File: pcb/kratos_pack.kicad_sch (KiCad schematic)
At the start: 94 parts, among them J1 USB_C_Receptacle_USB2.0, J2 PROG_CONN, J3 DBG_UART, J4 BAT_MID+NTC, J5 BAT_7.4V, J6 BAT_0V, J7 OUT+, J8 OUT-, Q1 AON7403, Q2 AON7414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

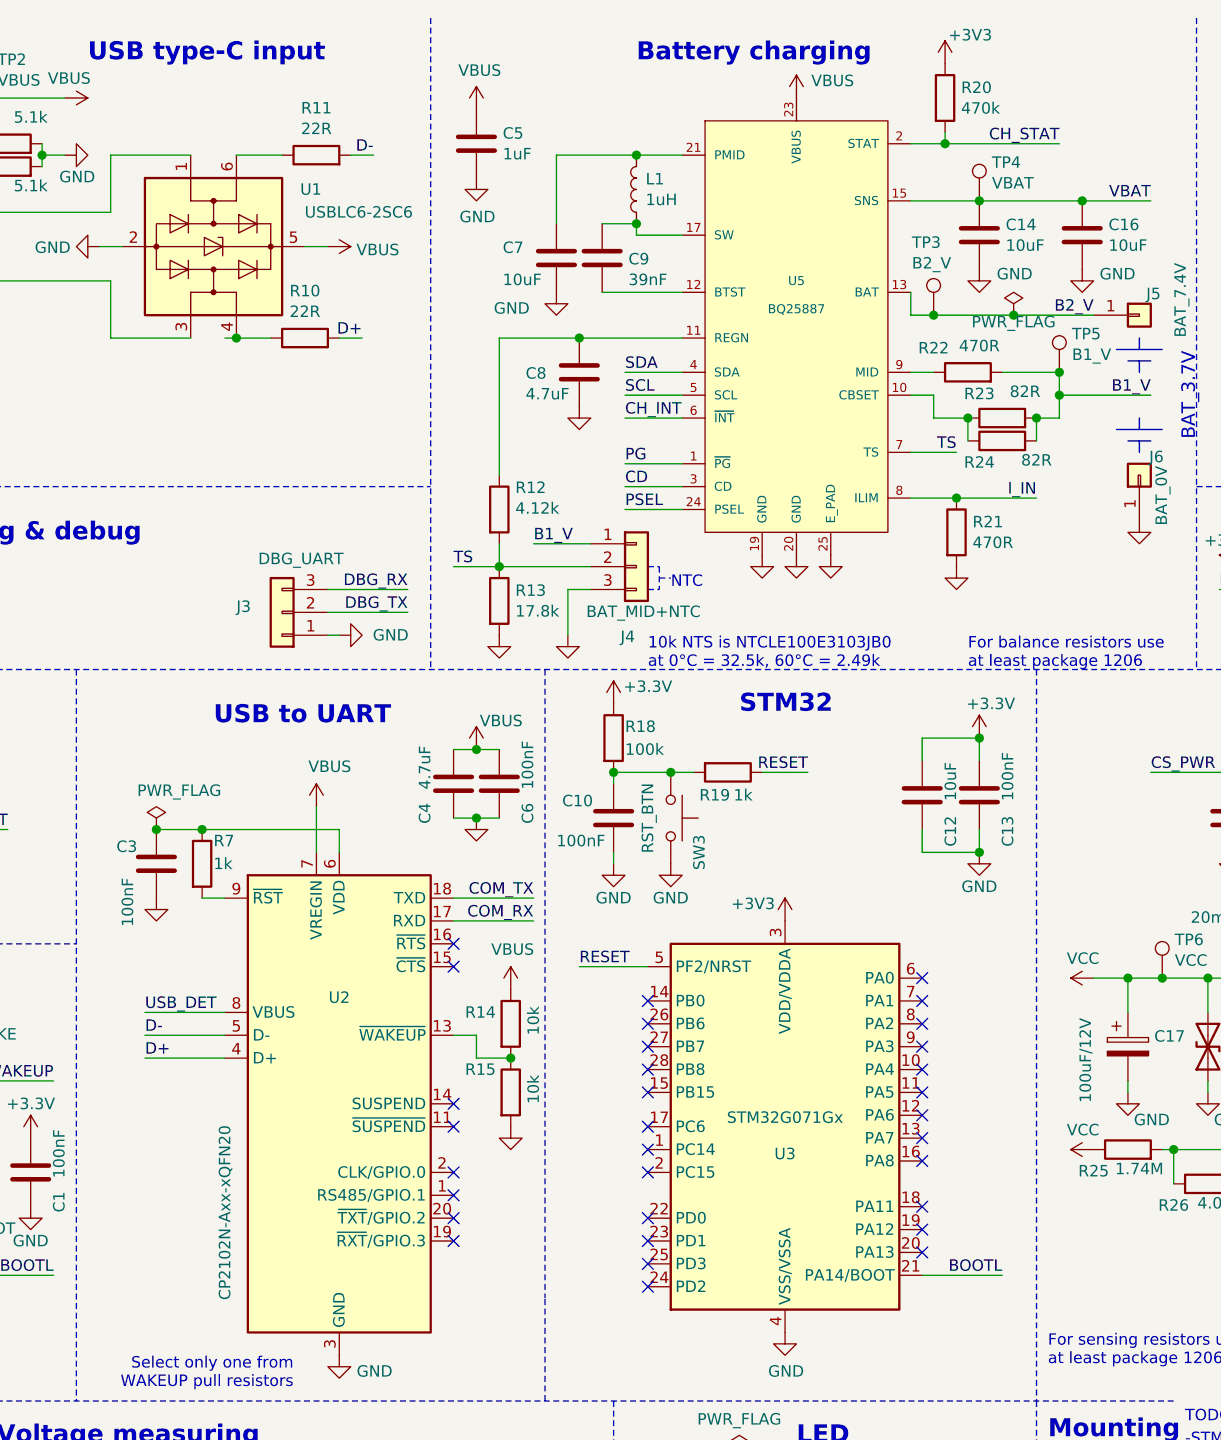
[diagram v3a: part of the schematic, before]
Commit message: Schema: add some connection STM32, remove redundant connections to BQ25887
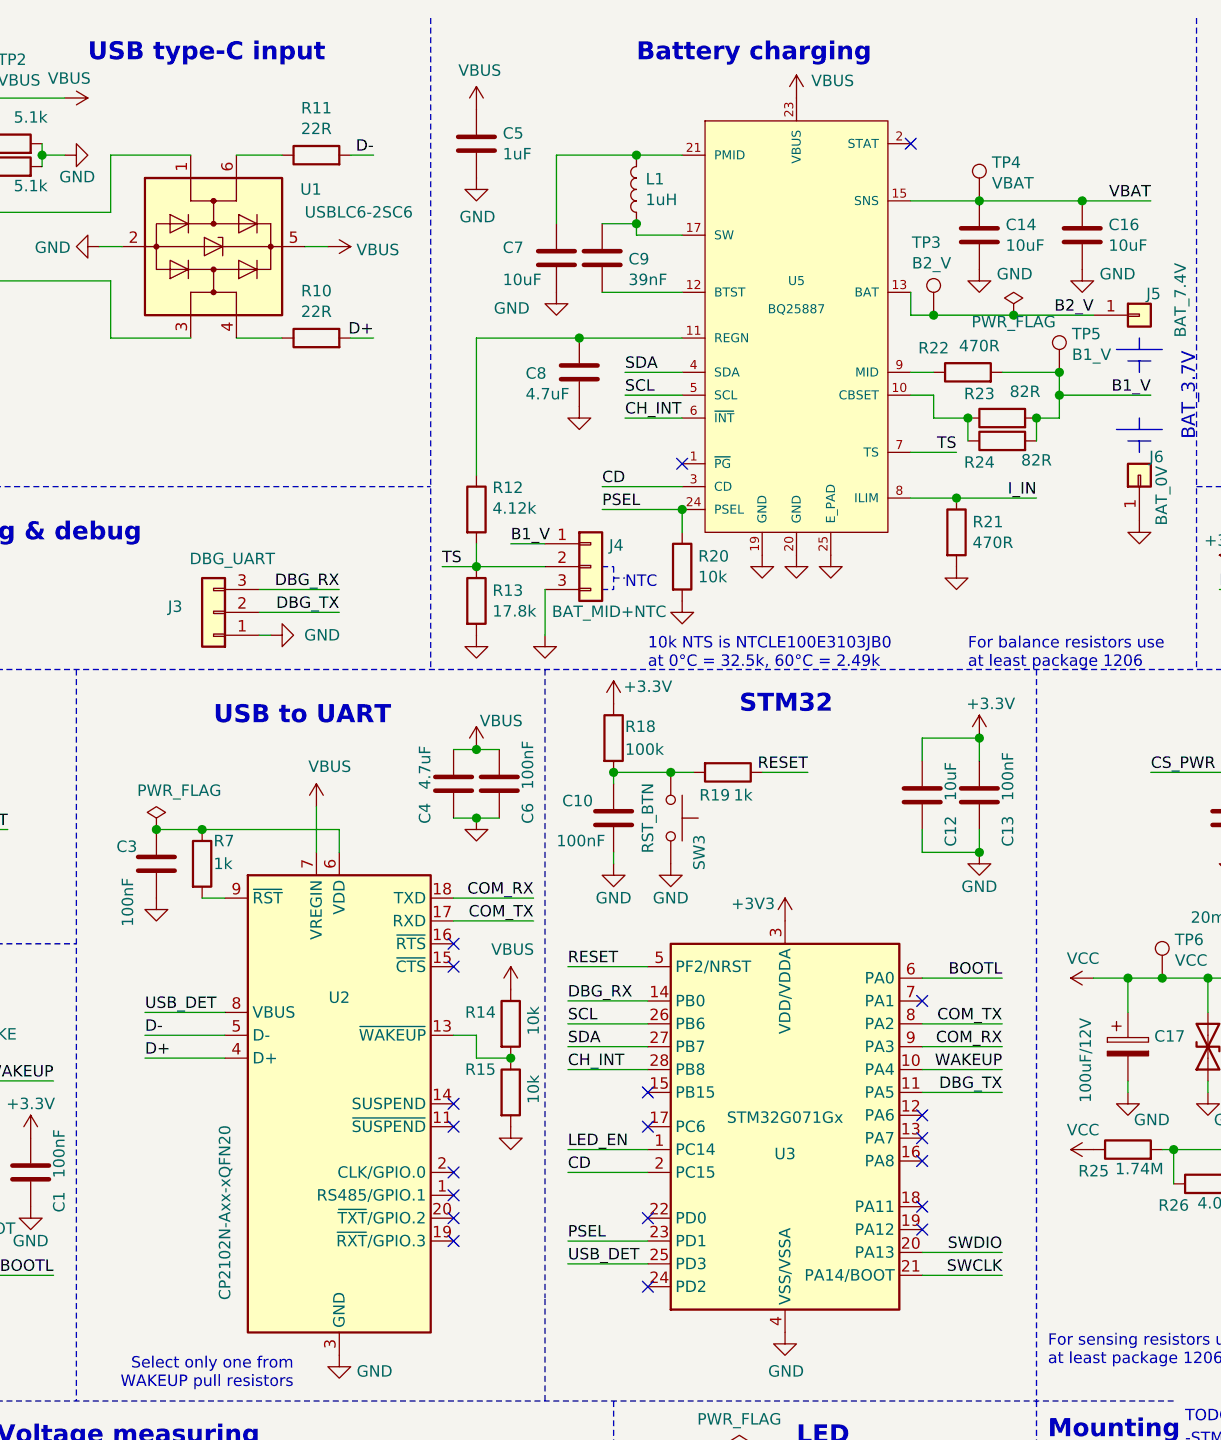
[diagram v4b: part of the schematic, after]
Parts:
- R20: value 470k -> 10k
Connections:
- net +3V3: no longer R20.1
- net BOOTL: now also U3.6 (PA0); no longer U3.21 (PA14/BOOT)
- net CD: now also U3.2 (PC15)
- net CH_INT: now also U3.28 (PB8)
- net COM_RX: now also U2.18 (TXD), U3.9 (PA3); no longer U2.17 (RXD)
- net COM_TX: now also U2.17 (RXD), U3.8 (PA2); no longer U2.18 (TXD)
- net DBG_RX: now also U3.14 (PB0)
- net DBG_TX: now also U3.11 (PA5)
- net GND: now also R20.2
- net LED_EN: now also U3.1 (PC14)
- net OUT_V: now also Q3.9 (D)
- net PSEL: now also R20.1, U3.23 (PD1)
- net SCL: now also U3.26 (PB6)
- net SDA: now also U3.27 (PB7)
- net SENSE: now also Q2.9 (D)
- net SWCLK: now also U3.21 (PA14/BOOT)
- net SWDIO: now also U3.20 (PA13)
- net USB_DET: now also U3.25 (PD3)
- net VCC: now also Q1.9 (D)
- net WAKEUP: now also U3.10 (PA4)
- net CH_STAT: no longer names the net of U5.2 (STAT)
- net CH_STAT: no longer R20.2
- net PG: no longer names the net of U5.1 (~PG)
- no-connect marks 35 -> 23
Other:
- moved on the sheet: J3, J4, R10, R12, R13, R20

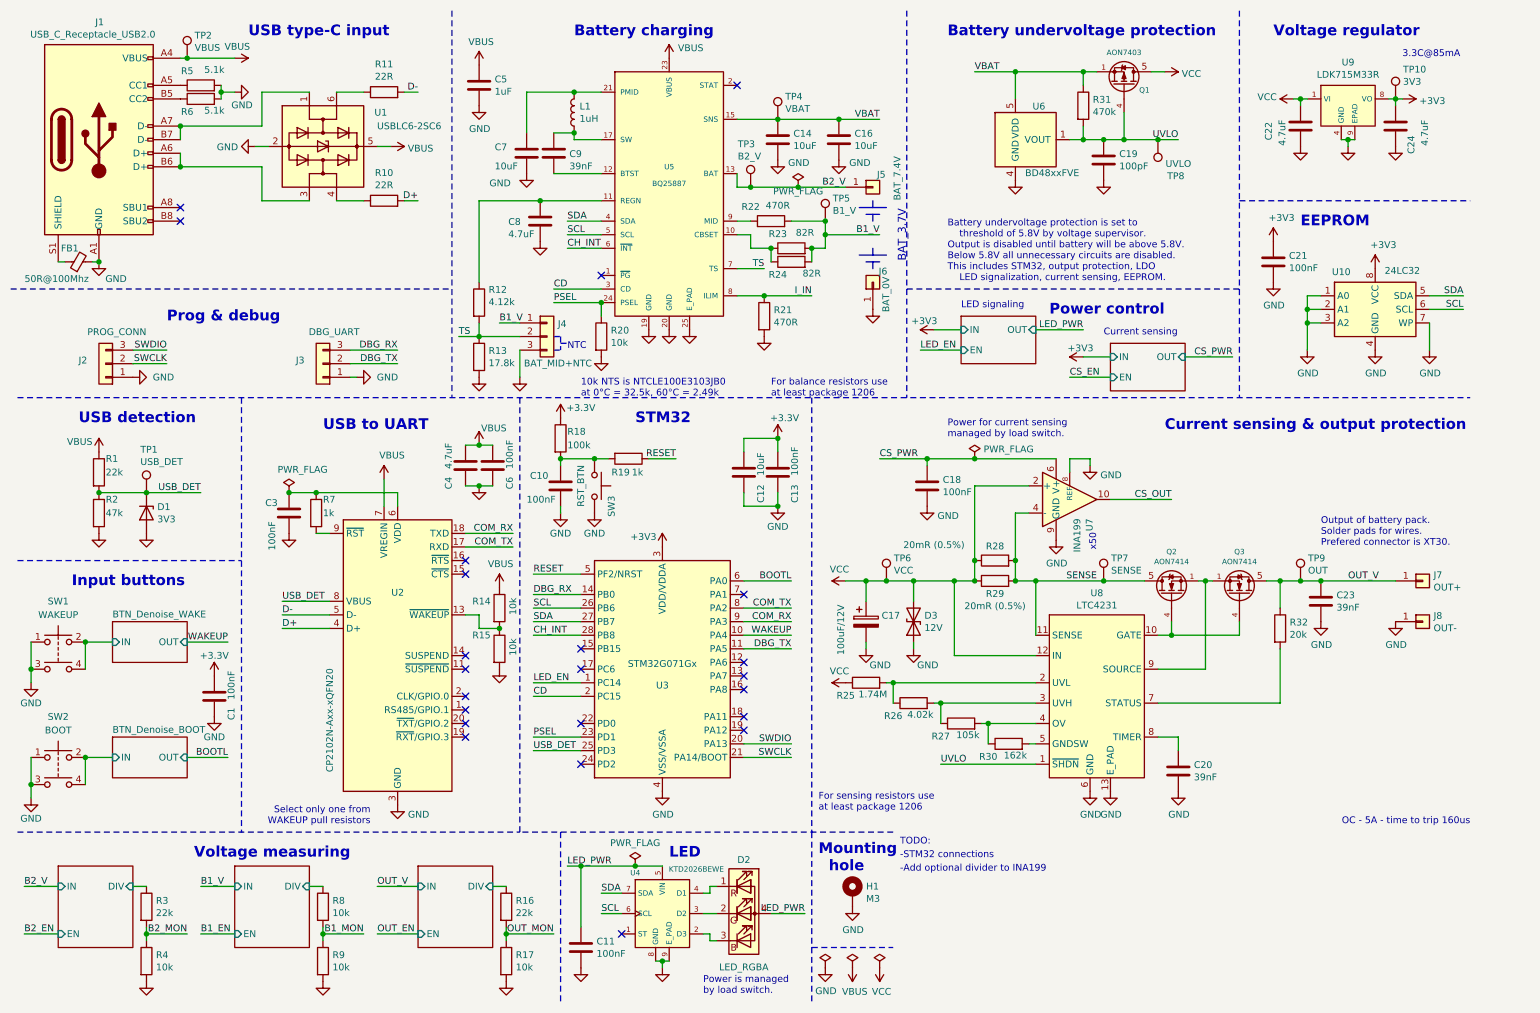
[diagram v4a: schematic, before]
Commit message: Schema: add connections from MCU to voltage measuring circuits
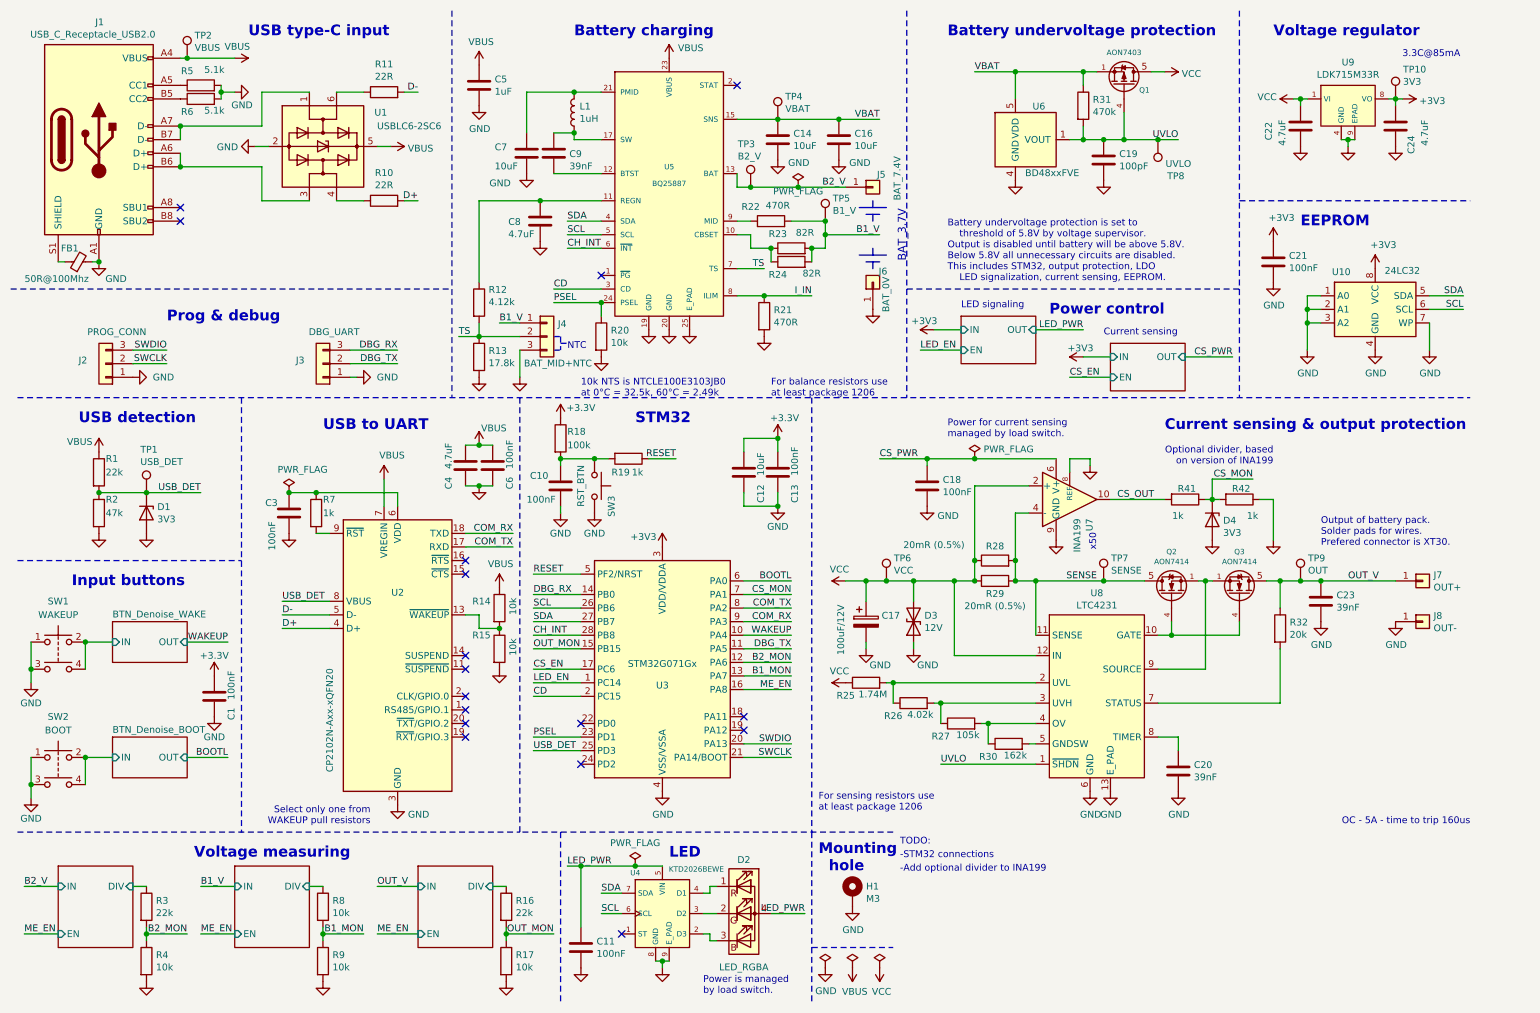
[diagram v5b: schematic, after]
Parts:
- added D4: 3V3, Diode_SMD:D_SOD-523, symbol Device:D_Zener
- added R41, R42: 1k, Resistor_SMD:R_0603_1608Metric, symbol Device:R
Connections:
- net B1_MON: now also U3.13 (PA7)
- net B2_MON: now also U3.12 (PA6)
- net CS_EN: now also U3.17 (PC6)
- net CS_OUT: now also R41.2
- net GND: now also D4.2 (A), R42.1
- net OUT_MON: now also U3.15 (PB15)
- net ME_EN: now reaches U3.16 (PA8)
- net CS_MON: now reaches U3.7 (PA1)
- net CS_MON: now also D4.1 (K), R41.1, R42.2
- no-connect marks 23 -> 17
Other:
- note added: "Optional divider, based on version of INA199"

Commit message: Schema: update connection of CS_EN pin
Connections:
- net CS_EN: now also U3.18 (PA11); no longer U3.17 (PC6)
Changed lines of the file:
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@@
   (no_connect (at 96.52 146.05))
   (no_connect (at 96.52 148.59))
+  (no_connect (at 118.11 135.89))
   (no_connect (at 118.11 146.05))
   (no_connect (at 118.11 153.67))
@@
   (no_connect (at 125.73 185.42))
   (no_connect (at 147.32 26.67))
-  (no_connect (at 148.59 144.78))
   (no_connect (at 148.59 147.32))
   (wire (pts (xy 13.97 176.53) (xy 20.32 176.53))
@@
     (stroke (width 0) (type solid) (color 0 0 0 0))
   )
-  (wire (pts (xy 109.22 135.89) (xy 118.11 135.89))
-    (stroke (width 0) (type solid) (color 0 0 0 0))
-  )
   (wire (pts (xy 109.22 138.43) (xy 118.11 138.43))
     (stroke (width 0) (type solid) (color 0 0 0 0))
@@
     (stroke (width 0) (type solid) (color 0 0 0 0))
   )
+  (wire (pts (xy 157.48 144.78) (xy 148.59 144.78))
+    (stroke (width 0) (type solid) (color 0 0 0 0))
+  )
   (wire (pts (xy 158.75 45.72) (xy 167.64 45.72))
     (stroke (width 0) (type solid) (color 0 0 0 0))
@@
     (effects (font (size 1.27 1.27)) (justify left bottom))
   )
-  (label "CS_EN" (at 109.22 135.89 0)
-    (effects (font (size 1.27 1.27)) (justify left bottom))
-  )
   (label "LED_EN" (at 109.22 138.43 0)
     (effects (font (size 1.27 1.27)) (justify left bottom))
@@
     (effects (font (size 1.27 1.27)) (justify right bottom))
   )
+  (label "CS_EN" (at 157.48 144.78 180)
+    (effects (font (size 1.27 1.27)) (justify right bottom))
+  )
   (label "SWDIO" (at 157.48 149.86 180)
     (effects (font (size 1.27 1.27)) (justify right bottom))
@@
     (stroke (width 0.001) (type solid) (color 132 0 132 1))
     (fill (color 72 72 72 1.0000))
-    (property "Sheet name" "BTN_Denoise_BOOT" (id 0) (at 30.48 147.9541 0)
+    (property "Název listu" "BTN_Denoise_BOOT" (id 0) (at 30.48 147.9541 0)
       (effects (font (size 1.27 1.27)) (justify left bottom))
     )
@@
     (stroke (width 0.001) (type solid) (color 132 0 132 1))
     (fill (color 72 72 72 1.0000))
-    (property "Sheet name" "BTN_Denoise_WAKE" (id 0) (at 30.48 126.3641 0)
+    (property "Název listu" "BTN_Denoise_WAKE" (id 0) (at 30.48 126.3641 0)
       (effects (font (size 1.27 1.27)) (justify left bottom))
     )
@@
     (stroke (width 0.001) (type solid) (color 132 0 132 1))
     (fill (color 72 72 72 1.0000))
-    (property "Sheet name" "Power_control" (id 0) (at 217.17 74.2941 0)
+    (property "Název listu" "Power_control" (id 0) (at 217.17 74.2941 0)
       (effects (font (size 1.27 1.27)) (justify left bottom) hide)
     )
@@
     (stroke (width 0.001) (type solid) (color 132 0 132 1))
     (fill (color 72 72 72 1.0000))
-    (property "Sheet name" "Power_control2" (id 0) (at 189.23 69.2141 0)
+    (property "Název listu" "Power_control2" (id 0) (at 189.23 69.2141 0)
       (effects (font (size 1.27 1.27)) (justify left bottom) hide)
     )
@@
     (stroke (width 0.001) (type solid) (color 132 0 132 1))
     (fill (color 72 72 72 1.0000))
-    (property "Sheet name" "Voltage_measuring" (id 0) (at 19.05 169.5441 0)
+    (property "Název listu" "Voltage_measuring" (id 0) (at 19.05 169.5441 0)
       (effects (font (size 1.27 1.27)) (justify left bottom) hide)
     )
@@
     (stroke (width 0.001) (type solid) (color 132 0 132 1))
     (fill (color 72 72 72 1.0000))
-    (property "Sheet name" "Voltage_measuring1" (id 0) (at 52.07 169.5441 0)
+    (property "Název listu" "Voltage_measuring1" (id 0) (at 52.07 169.5441 0)
       (effects (font (size 1.27 1.27)) (justify left bottom) hide)
     )
@@
     (stroke (width 0.001) (type solid) (color 132 0 132 1))
     (fill (color 72 72 72 1.0000))
-    (property "Sheet name" "Voltage_measuring2" (id 0) (at 86.36 169.5441 0)
+    (property "Název listu" "Voltage_measuring2" (id 0) (at 86.36 169.5441 0)
       (effects (font (size 1.27 1.27)) (justify left bottom) hide)
     )

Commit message: Schema: update page layout
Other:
- note removed: "-Add optional divider to INA199"
- note removed: "-STM32 connections"
- note removed: "TODO:"
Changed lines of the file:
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@@
     (title "Kratos pack")
     (date "2020-12-18")
-    (rev "v0.1")
+    (rev "v1.0")
     (company "Author: Petr Malaník")
   )
@@
     (effects (font (size 2 2) (thickness 0.4) bold) (justify left bottom))
   )
-  (text "TODO:" (at 177.8 168.91 0)
-    (effects (font (size 1.27 1.27)) (justify left bottom))
-  )
-  (text "-STM32 connections" (at 177.8 171.45 0)
-    (effects (font (size 1.27 1.27)) (justify left bottom))
-  )
-  (text "-Add optional divider to INA199\n" (at 177.8 173.99 0)
-    (effects (font (size 1.27 1.27)) (justify left bottom))
-  )
   (text "BAT_3.7V" (at 179.07 59.69 90)
